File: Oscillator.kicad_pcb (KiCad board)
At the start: 2 copper layers, 43.5 x 75 mm, 62 parts, among them P202 CONN_2, P203 CONN_2, P301 CONN_2, P302 CONN_2, SW201 SPST, SW301 SPST, U201 TL072, U301 TL072

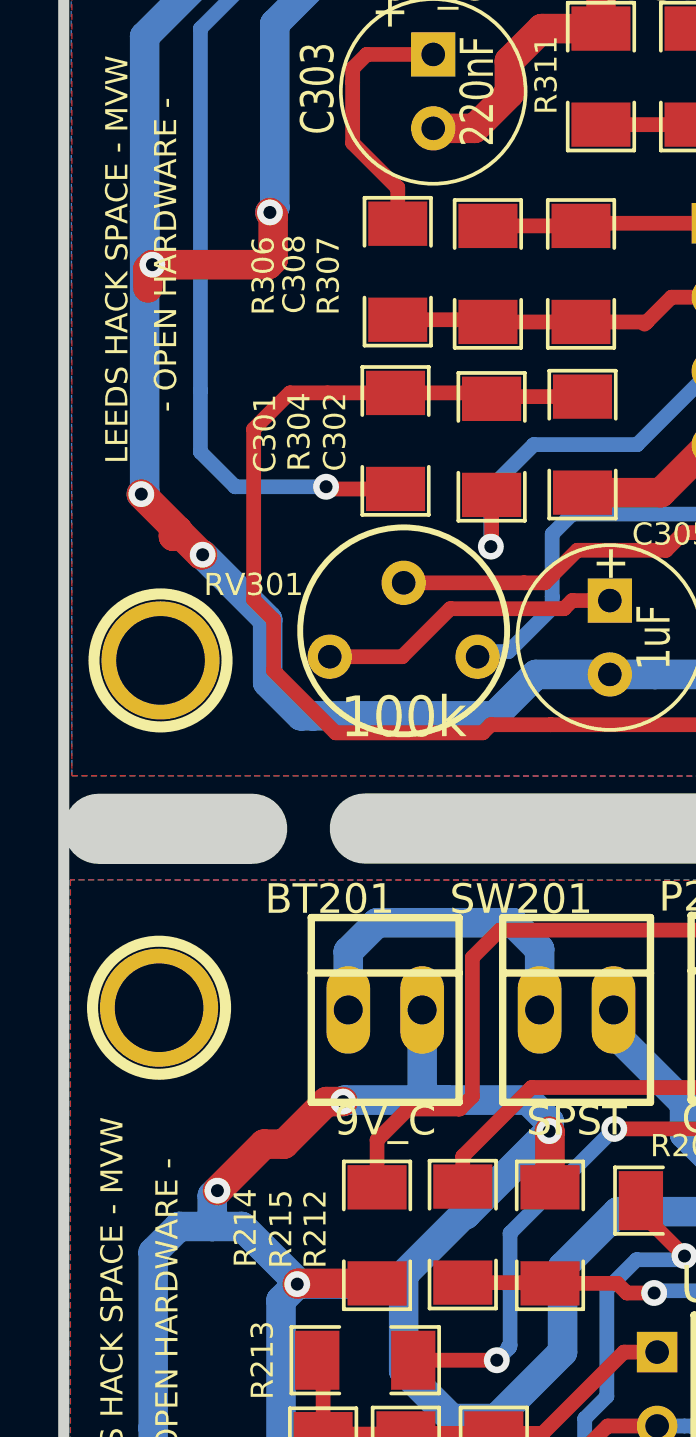
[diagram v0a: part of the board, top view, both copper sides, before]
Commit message: committing some library updates and sims along with a bom
committing some library updates and sims along with a bom.
These were updated quite a while ago so i'm not sure if this information
is accurate or correct.
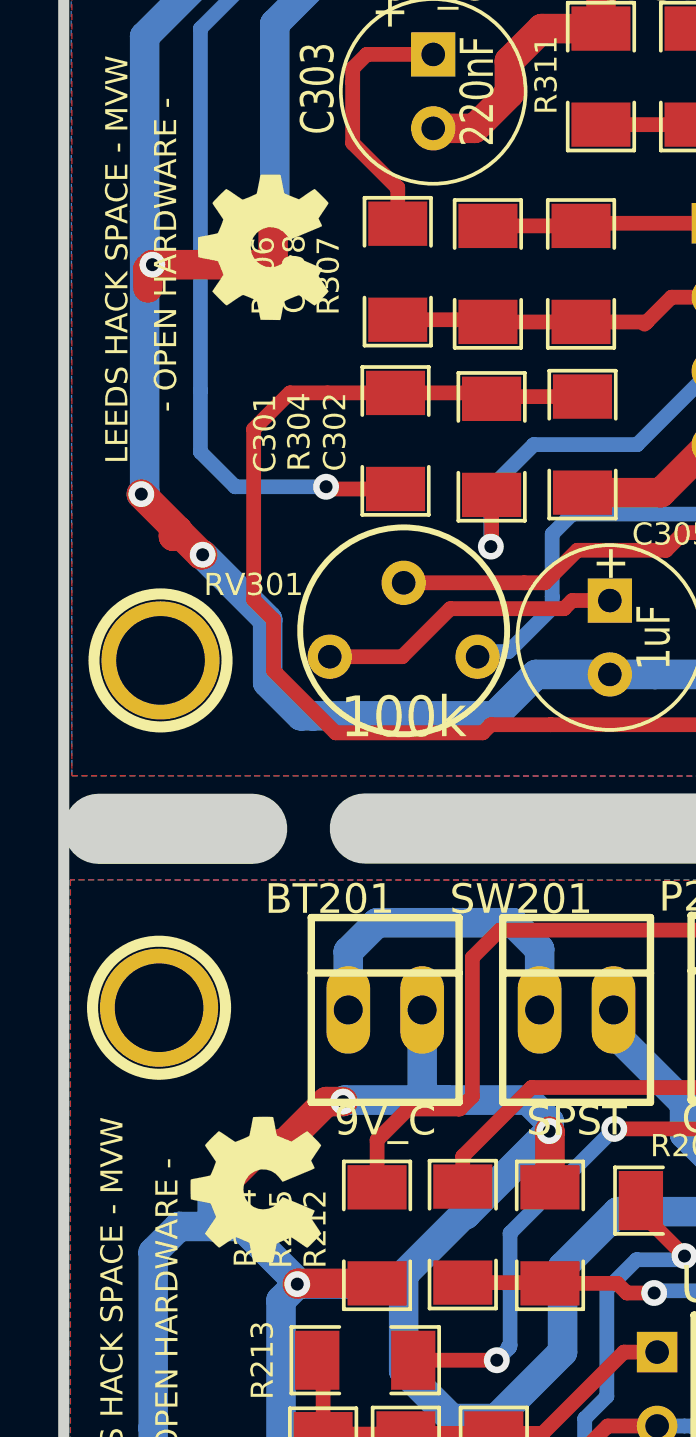
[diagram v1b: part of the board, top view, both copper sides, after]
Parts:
- added G***: OSHW-logo_silkscreen-front_5mm, OSHW-logo_silkscreen-front_5mm, F.Cu at (148.7, 95.0)
- added G***: OSHW-logo_silkscreen-front_5mm, OSHW-logo_silkscreen-front_5mm, F.Cu at (149.0, 62.6)
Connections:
- C202 pad 1: N-000009 (its old number) -> /RelaxationOscillator/IN2-
- R209 pad 2: N-000009 (its old number) -> /RelaxationOscillator/IN2-
- R210 pad 1: N-000009 (its old number) -> /RelaxationOscillator/IN2-
- U201 pad 5: N-000009 (its old number) -> /RelaxationOscillator/IN2-
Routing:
- net N-000009 (its old number): track 25.4 -> 0.00 mm
- net /RelaxationOscillator/IN2-: track 0.00 -> 25.4 mm
